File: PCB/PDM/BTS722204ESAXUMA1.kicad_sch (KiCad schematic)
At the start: 22 parts, among them IC7 BTS722204ESAXUMA1

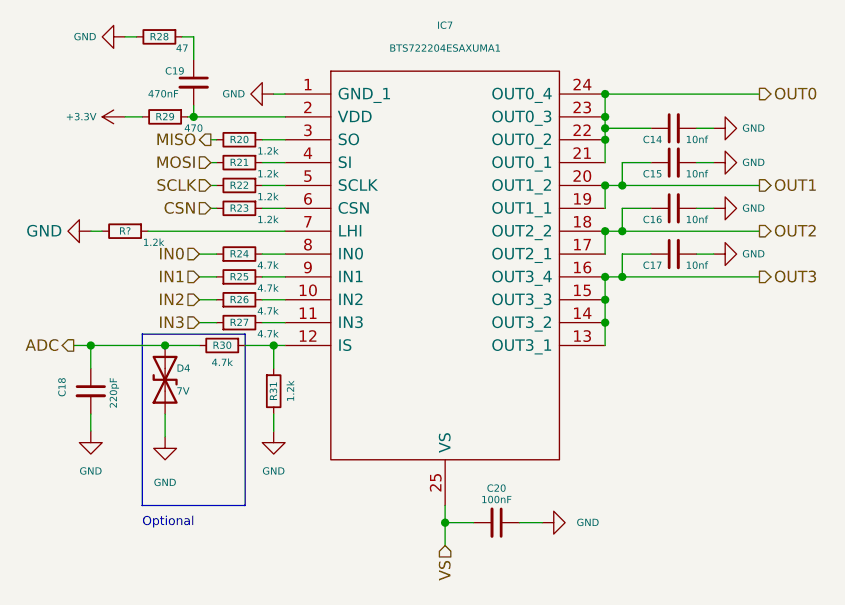
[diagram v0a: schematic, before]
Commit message: Added Reverse polarity protection
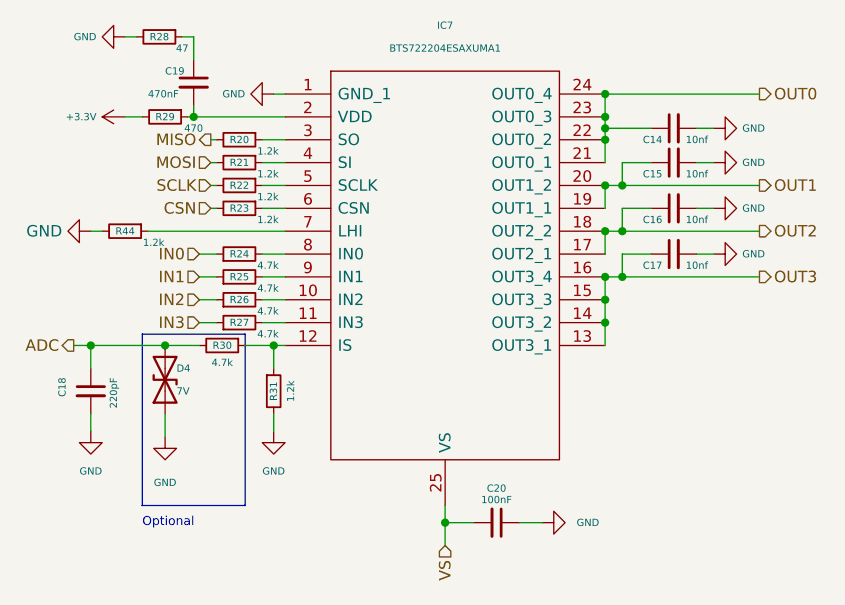
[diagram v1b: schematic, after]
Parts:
- gave numbers to parts that had none: 1
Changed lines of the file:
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@@
   (symbol (lib_id "power:GND") (at 38.735 58.42 270) (unit 1)
     (in_bom yes) (on_board yes) (fields_autoplaced)
-    (property "Reference" "#PWR?" (id 0) (at 32.385 58.42 0)
+    (property "Reference" "#PWR0147" (id 0) (at 32.385 58.42 0)
       (effects (font (size 1.27 1.27)) hide)
     )
@@
   (symbol (lib_id "Device:R_Small") (at 42.545 58.42 270) (unit 1)
     (in_bom yes) (on_board yes)
-    (property "Reference" "R?" (id 0) (at 42.545 58.42 90)
+    (property "Reference" "R44" (id 0) (at 42.545 58.42 90)
       (effects (font (size 0.8 0.8)))
     )
